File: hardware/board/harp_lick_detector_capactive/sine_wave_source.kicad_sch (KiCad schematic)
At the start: 15 parts, among them U3 ADA4807-2ARM, U4 AD9833xRM, X1 ASE-25.000MHZ-L-C-T

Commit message: document stray capacitances
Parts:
- removed U3: ADA4807-2ARM, symbol Amplifier_Operational:ADA4807-2ARM
- added C41, C42: 100pF, Capacitor_SMD:C_0603_1608Metric_Pad1.08x0.95mm_HandSolder, symbol Device:C
- added R34: 316K, symbol Device:R
- added R35: 1M13, symbol Device:R
- added R36: 226, symbol Device:R
- added U10: OPA4354, symbol machine_agency_components:OPA4354
- gave numbers to parts that had none: 11
- renumbered U4 to U7, X1 to X2
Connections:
- net +2V5: now also U10.4 (V+)
- net -2V5: now also U10.11 (V-)
- net GNDA: now also C41.1, R35.1
- net VSIN: now also R36.1, U10.8, U10.9 (-)
- net at R18.2, R19.1, RV2.1: now also U10.5 (+)
- new net: C41.2, C42.2, R34.2, R36.2
- new net: C42.1, R35.2, U10.10 (+)
- new net: R34.1, U10.6 (-), U10.7
- no-connect marks 1 -> 4
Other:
- note added: "Band Pass Filter to remove DC offset and attenuate quantization artifact. Fc = 15[KHz]"
- note added: "OPA4354 Bypass Caps"
- note removed: "ADA4807-2 Bypass Caps"
- note removed: "High Pass Filter to remove DC offset. Fc = 15[KHz]"
- moved on the sheet: C32, R20

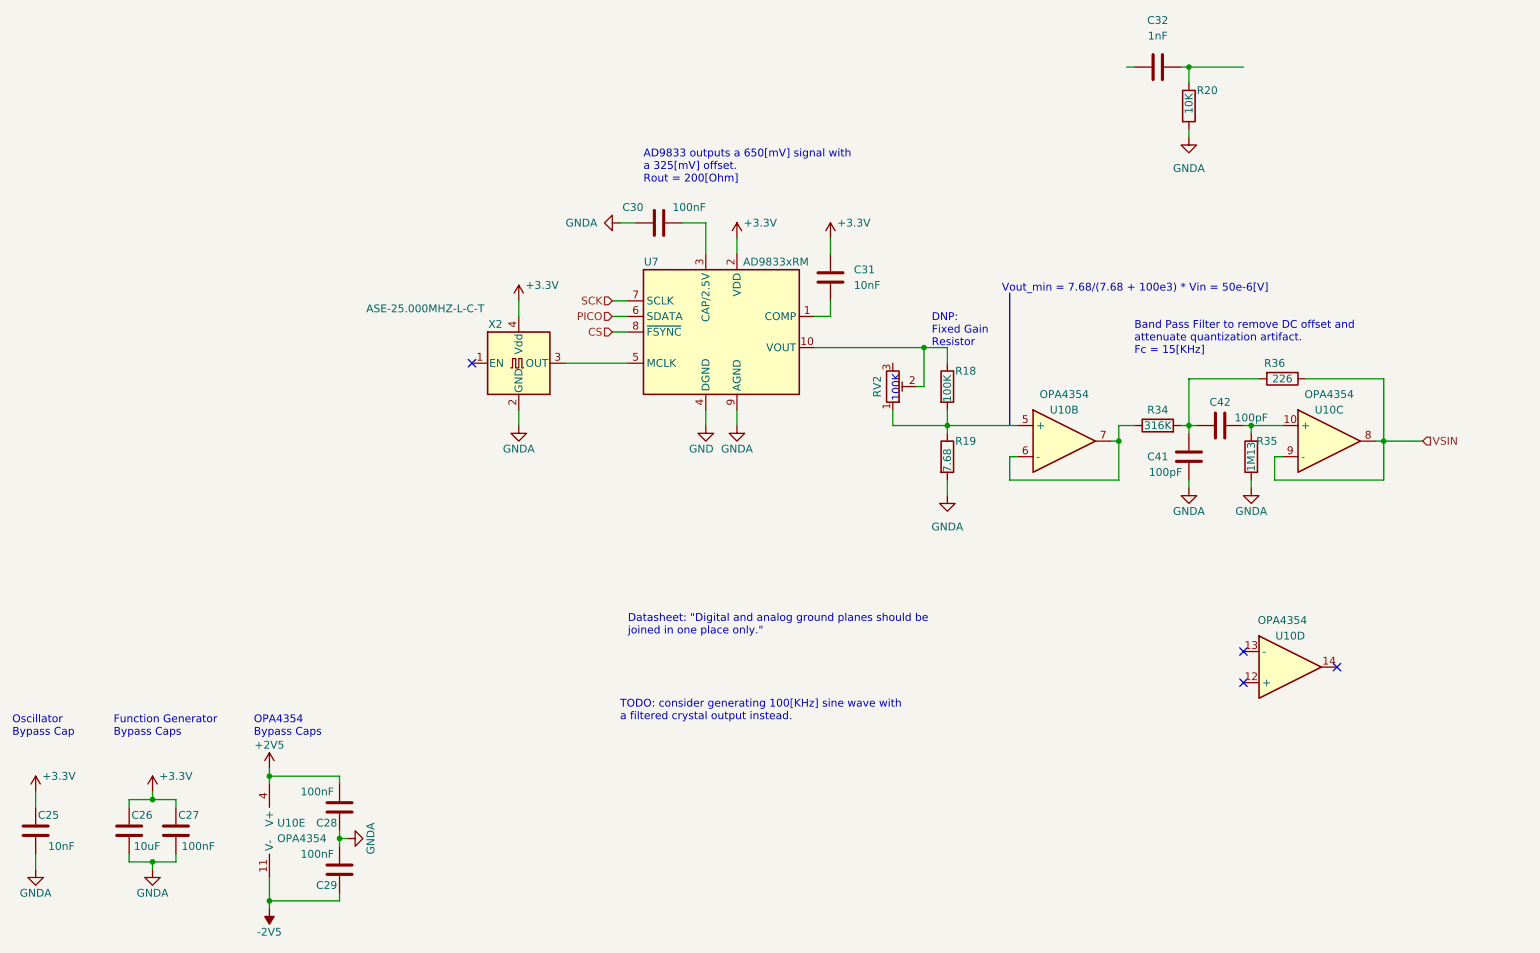
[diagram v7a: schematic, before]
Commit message: pass eeschema drc
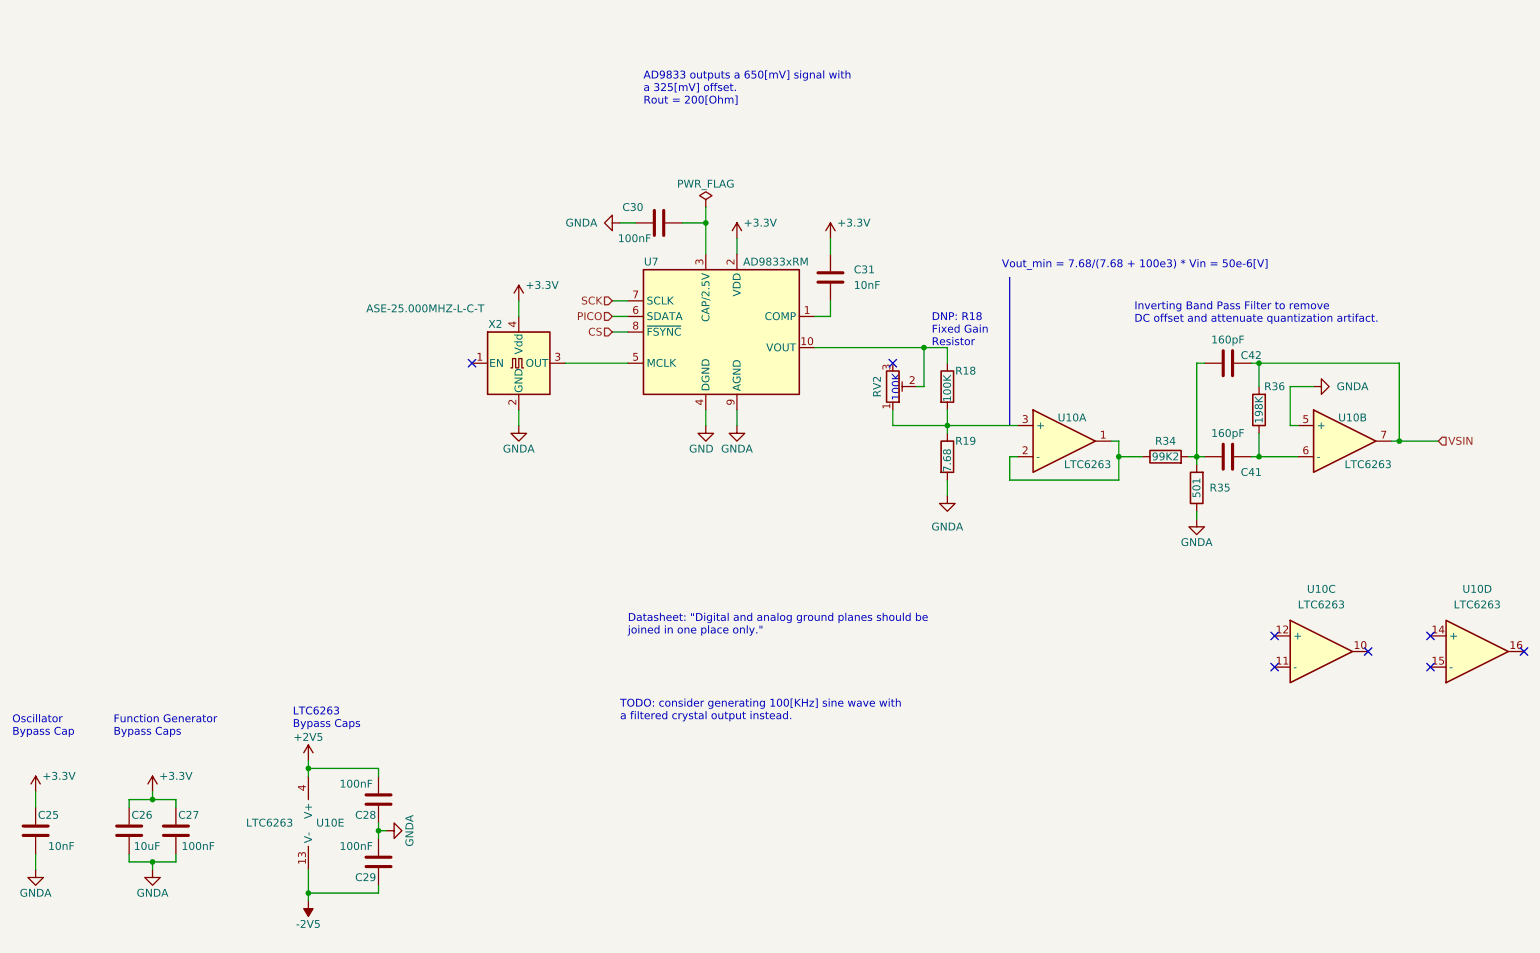
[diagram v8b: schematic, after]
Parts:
- removed C32: 1nF, symbol Device:C
- removed R20: 10K, Resistor_SMD:R_0402_1005Metric_Pad0.72x0.64mm_HandSolder, symbol Device:R
- removed U10: OPA4354, symbol machine_agency_components:OPA4354
- added U10: LTC6263, Package_SO:MSOP-16_3x4mm_P0.5mm, symbol machine_agency_components:LTC6263
- C41, C42: value 100pF -> 160pF; footprint Capacitor_SMD:C_0603_1608Metric_Pad1.08x0.95mm_HandSolder -> Capacitor_SMD:C_0402_1005Metric_Pad0.74x0.62mm_HandSolder; Link https://www.digikey.com/en/products/detail/murata-electronics/GRM033R71E101JA01D/10703869 -> https://www.digikey.com/en/products/detail/murata-electronics/GCM1555C1H161FA16D/11618546; Manufacturer Number GRM033R71E101JA01D -> GCM1555C1H161FA16D; Rated Voltage 25V -> 50V; Temperature Coefficient X7R -> C0G, NP0; Tolerance 5% -> 1%
- R34: value 316K -> 99K2
- R35: value 1M13 -> 501
- R36: value 226 -> 198K
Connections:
- net +2V5: now also U10.4 (V+)
- net -2V5: now also U10.13 (V-)
- net GNDA: now also U10.5 (+); no longer C41.1
- net VSIN: now also C42.2, R36.2, U10.7; no longer R36.1
- net at R18.2, R19.1, RV2.1: now also U10.3 (+)
- net at C42.1, R35.2: now also C41.1, R34.2
- net at R34.1: now also U10.1, U10.2 (-)
- new net: C41.2, R36.1, U10.6 (-)
- no-connect marks 4 -> 8
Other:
- note added: "DNP: R18 Fixed Gain Resistor"
- note added: "Inverting Band Pass Filter to remove DC offset and attenuate quantization artifact."
- note added: "LTC6263 Bypass Caps"
- note removed: "Band Pass Filter to remove DC offset and attenuate quantization artifact. Fc = 15[KHz]"
- note removed: "DNP: Fixed Gain Resistor"
- note removed: "OPA4354 Bypass Caps"
- moved on the sheet: C28, C29
